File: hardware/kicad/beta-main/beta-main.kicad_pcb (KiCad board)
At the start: 4 copper layers, 76 x 121 mm, 55 parts, among them J1 FFC3A20-15-G, J10 Servo Socket, J11 Servo Socket, J12 Servo Socket, J2 FFC3A20-15-G, J3 XT60, J4 Conn_01x04_Pin, J8 Conn_01x02_Socket, J9 Servo Socket, Q2 MMBT3906, U1 MAX98357A, U2 TPS56624x, U3 AP3441SHE-7B, U6 BNO086, U7 74LVC1G126, U8 74LVC1G126

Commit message: add modifications
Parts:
- removed Module1: ComputeModule5-CM5, CM5IO:Raspberry-Pi-5-Compute-Module
- removed R14, R15: 10k, Resistor_SMD:R_0402_1005Metric
- removed U8: 74LVC1G126, Package_TO_SOT_SMD:SOT-23-5
- added C20: 10u, Capacitor_SMD:C_0603_1608Metric_Pad1.08x0.95mm_HandSolder, F.Cu at (249.1, 52.2)
- added C3: 10u, Capacitor_SMD:C_0603_1608Metric_Pad1.08x0.95mm_HandSolder, F.Cu at (240.4, 47.2)
- added C4: 10u, Capacitor_SMD:C_0603_1608Metric_Pad1.08x0.95mm_HandSolder, F.Cu at (240.4, 49.7)
- added CM5: ComputeModule5-CM5, CM5IO:Raspberry-Pi-5-Compute-Module, F.Cu at (83.5, 124.0)
- added D1: LED_RED, LED_SMD:LED_0603_1608Metric, F.Cu at (184.2, 109.0)
- added D2: 1N5819WS, Diode_SMD:D_SOD-323, F.Cu at (177.4, 113.6)
- added J13: Servo Socket, Connector_JST:JST_XH_S3B-XH-A_1x03_P2.50mm_Horizontal, F.Cu at (128.1, 150.0)
- added J14: Conn_01x04_Pin, Connector_JST:JST_PH_S4B-PH-K_1x04_P2.00mm_Horizontal, F.Cu at (69.0, 49.5)
- added J15: Conn_01x04_Pin, Connector_JST:JST_PH_S4B-PH-K_1x04_P2.00mm_Horizontal, F.Cu at (131.1, 55.5)
- added J16: Conn_01x04_Pin, Connector_JST:JST_PH_S4B-PH-K_1x04_P2.00mm_Horizontal, F.Cu at (131.1, 139.5)
- added J17: Conn_01x04_Pin, Connector_JST:JST_PH_S4B-PH-K_1x04_P2.00mm_Horizontal, F.Cu at (69.0, 133.5)
- added J18: XT60, Connector_AMASS:AMASS_XT60-F_1x02_P7.20mm_Vertical, F.Cu at (151.5, 152.5)
- added J19: FAN0, Connector_JST:JST_PH_B2B-PH-K_1x02_P2.00mm_Vertical, F.Cu at (116.0, 149.4)
- added J20: FAN1, Connector_JST:JST_PH_B2B-PH-K_1x02_P2.00mm_Vertical, F.Cu at (80.5, 149.4)
- added J21: PWR, Connector_JST:JST_PH_B2B-PH-K_1x02_P2.00mm_Vertical, F.Cu at (122.5, 50.0)
- added J5: DSI, Connector_FFC-FPC:TE_1-84953-5_1x15-1MP_P1.0mm_Horizontal, F.Cu at (130.7, 100.0)
- added J6: USB3_A, BETA:22009L012N1, F.Cu at (171.8, 77.5)
- added J7: USB3-1, Connector_JST:JST_PH_B8B-PH-K_1x08_P2.00mm_Vertical, F.Cu at (170.3, 101.8)
- added MH10: M2.5, MountingHole:MountingHole_2.7mm_Pad, F.Cu at (129.0, 75.5)
- added MH11: M2.5, MountingHole:MountingHole_2.7mm_Pad, F.Cu at (71.0, 124.5)
- added MH12: M2.5, MountingHole:MountingHole_2.7mm_Pad, F.Cu at (129.0, 124.5)
- added MH9: M2.5, MountingHole:MountingHole_2.7mm_Pad, F.Cu at (71.0, 75.5)
- added Q1: MMBT3906, Package_TO_SOT_SMD:SOT-23, F.Cu at (198.9, 54.6)
- added R10: 10K 1%, Resistor_SMD:R_0402_1005Metric, F.Cu at (260.8, 52.3)
- added R6: 100K 1%, Resistor_SMD:R_0402_1005Metric, F.Cu at (260.8, 44.4)
- added R7: 220K, Resistor_SMD:R_0402_1005Metric, F.Cu at (260.8, 46.4)
- added R8: 30K, Resistor_SMD:R_0402_1005Metric, F.Cu at (260.8, 48.4)
- added R9: 15k, Resistor_SMD:R_0402_1005Metric, F.Cu at (260.8, 50.4)
- added REF**: LayerMarker_4_6.35x2.54mm_TextH1mm_P1.27mm, Symbol:LayerMarker_4_6.35x2.54mm_TextH1mm_P1.27mm, F.Cu at (77.0, 52.5)
- added U4: 74LVC1G126, Package_TO_SOT_SMD:SOT-23-5, F.Cu at (69.1, 103.0)
- added U5: AP3441SHE-7B, Package_DFN_QFN:DFN-8-1EP_2x2mm_P0.5mm_EP1.05x1.75mm, F.Cu at (110.9, 144.2)
- C1: value 220u -> 0.1u
- C10: value 22u -> 4.7nF; footprint Capacitor_SMD:C_0603_1608Metric_Pad1.08x0.95mm_HandSolder -> Capacitor_SMD:C_0402_1005Metric
- C12: value 10u -> 100u
- C14: value 0.1u -> 22u; footprint Capacitor_SMD:C_0402_1005Metric -> Capacitor_SMD:C_0603_1608Metric_Pad1.08x0.95mm_HandSolder
- C15: value 4.7nF -> 10u; footprint Capacitor_SMD:C_0402_1005Metric -> Capacitor_SMD:C_0603_1608Metric_Pad1.08x0.95mm_HandSolder
- C17, C19: value 10u -> 22u
- C2: value 0.1u -> 220u
- C8: value 22u -> 0.1u; footprint Capacitor_SMD:C_0603_1608Metric_Pad1.08x0.95mm_HandSolder -> Capacitor_SMD:C_0402_1005Metric
- C9: value 22u -> 10u
- J1: value FFC3A20-15-G -> AUDIO; footprint Connector_FFC-FPC:TE_1-84953-5_1x15-1MP_P1.0mm_Horizontal -> Connector_JST:JST_PH_B2B-PH-K_1x02_P2.00mm_Vertical
- J10, J11, J12: footprint Connector_JST:JST_XH_B3B-XH-AM_1x03_P2.50mm_Vertical -> Connector_JST:JST_XH_S3B-XH-A_1x03_P2.50mm_Horizontal
- J2: value FFC3A20-15-G -> USB3-0; footprint Connector_FFC-FPC:TE_1-84953-5_1x15-1MP_P1.0mm_Horizontal -> Connector_JST:JST_PH_B8B-PH-K_1x08_P2.00mm_Vertical
- J3: value XT60 -> USB3-1; footprint Connector_AMASS:AMASS_XT60-F_1x02_P7.20mm_Vertical -> Connector_JST:JST_PH_B8B-PH-K_1x08_P2.00mm_Vertical
- J4: value Conn_01x04_Pin -> USB3-1; footprint Connector_JST:JST_XH_B4B-XH-AM_1x04_P2.50mm_Vertical -> Connector_JST:JST_PH_B8B-PH-K_1x08_P2.00mm_Vertical
- J8: value Conn_01x02_Socket -> CSI; footprint Connector_PinHeader_2.54mm:PinHeader_1x02_P2.54mm_Vertical -> Connector_FFC-FPC:TE_1-84953-5_1x15-1MP_P1.0mm_Horizontal
- J9: value Servo Socket -> USB3_A; footprint Connector_JST:JST_XH_B3B-XH-AM_1x03_P2.50mm_Vertical -> BETA:22009L012N1
- Q2: value MMBT3906 -> IRLML6246TRP
- R1: value 220K -> 20k
- R11: value 20k -> 2.2K 1%
- R12: value 10k -> 1k; footprint Resistor_SMD:R_0402_1005Metric -> Resistor_SMD:R_0603_1608Metric
- R13: footprint Resistor_SMD:R_0402_1005Metric -> Resistor_SMD:R_0603_1608Metric
- R2: value 30K -> 10k
- R3: value 100K 1% -> 10k
- R4: value 10K 1% -> 10k
- R5: value 2.2K 1% -> 10k
- U2: value TPS56624x -> 74LVC1G126; footprint Package_TO_SOT_SMD:SOT-563 -> Package_TO_SOT_SMD:SOT-23-5
- U3: value AP3441SHE-7B -> BNO086; footprint Package_DFN_QFN:DFN-8-1EP_2x2mm_P0.5mm_EP1.05x1.75mm -> BETA:IC_BNO086
- U6: value BNO086 -> TPS56624x; footprint BNO086:IC_BNO086 -> Package_TO_SOT_SMD:SOT-563
- U7: value 74LVC1G126 -> AP2553W6; footprint Package_TO_SOT_SMD:SOT-23-5 -> Package_TO_SOT_SMD:SOT-23-6
- moved TP2 201.8 mm to (257.3, 37.7)
- moved C17 192.6 mm to (249.1, 44.6), turned to 0 degrees
- moved C18 192.1 mm to (249.1, 47.2), turned to 0 degrees
- moved C19 191.5 mm to (249.1, 49.7), turned to 0 degrees
- moved C12 188.3 mm to (244.8, 47.2), turned to 0 degrees
- moved R11 187.8 mm to (260.8, 54.3), turned to 0 degrees
- moved C13 185.2 mm to (244.8, 49.7), turned to 0 degrees
- moved L2 184.0 mm to (255.3, 54.1)
- moved C14 183.7 mm to (244.8, 52.2)
- moved C10 182.3 mm to (260.3, 38.1), turned to 0 degrees
- moved C16 181.7 mm to (244.8, 57.2), turned to 0 degrees
- moved C8 181.7 mm to (260.3, 36.1), turned to 0 degrees
- moved C15 180.8 mm to (244.8, 54.7)
- moved TP1 178.2 mm to (257.3, 34.7)
- moved C7 174.6 mm to (260.3, 34.1), turned to 0 degrees
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- renumbered MH2 to MH3, MH3 to MH5, MH4 to MH7
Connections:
- C1 pad 1: +BATT -> GND
- C1 pad 2: GND -> Net-(U3-CAP)
- C10 pad 1: +5V -> +3V3
- C10 pad 2: GND -> /PSU/FB
- C12 pad 1: +5V -> VBUS
- C13 pad 1: +5V -> +3V3
- C15 pad 1: +3V3 -> VBUS
- C15 pad 2: /PSU/3V3/FB -> GND
- C17 pad 1: +3V3 -> +5V
- C19 pad 1: +3V3 -> +5V
- C2 pad 1: GND -> +BATT
- C2 pad 2: Net-(U6-CAP) -> GND
- C5 pad 1: +BATT -> +5V
- C7 pad 1: +BATT -> +5V
- C8 pad 1: +5V -> +BATT
- J1 pad 1: GND -> Net-(J1-Pin_1)
- J1 pad 2: /CM5/MIPI0_D1_N -> Net-(J1-Pin_2)
- J10 pad 1: Net-(J10-Pin_1) -> /Peripherals/SIG
- J11 pad 1: Net-(J10-Pin_1) -> /Peripherals/SIG
- J12 pad 1: Net-(J10-Pin_1) -> /Peripherals/SIG
- J2 pad 1: GND -> VBUS
- J2 pad 2: /CM5/MIPI1_D0_N -> /High Speed Serial/USB3-0-D_N
- J2 pad 3: /CM5/MIPI1_D0_P -> /High Speed Serial/USB3-0-D_P
- J2 pad 4: GND -> /High Speed Serial/USB3-0-RX_N
- J2 pad 5: /CM5/MIPI1_D1_N -> /High Speed Serial/USB3-0-RX_P
- J2 pad 6: /CM5/MIPI1_D1_P -> /High Speed Serial/USB3-0-TX_N
- J2 pad 7: GND -> /High Speed Serial/USB3-0-TX_P
- J2 pad 8: /CM5/MIPI1_C_N -> GND
- J3 pad 1: GND -> VBUS
- J3 pad 2: +BATT -> /High Speed Serial/USB3-1-D_N
- J4 pad 1: unconnected-(J4-Pin_1-Pad1) -> Net-(J4-Pin_1)
- J4 pad 2: unconnected-(J4-Pin_2-Pad2) -> Net-(J4-Pin_2)
- J4 pad 3: unconnected-(J4-Pin_3-Pad3) -> Net-(J4-Pin_3)
- J4 pad 4: unconnected-(J4-Pin_4-Pad4) -> Net-(J4-Pin_4)
- J8 pad 1: Net-(J8-Pin_1) -> GND
- J8 pad 2: Net-(J8-Pin_2) -> /MIPI1_D0_N
- J9 pad 1: Net-(J10-Pin_1) -> Net-(J7-Pin_1)
- J9 pad 2: +BATT -> Net-(J7-Pin_2)
- J9 pad 3: GND -> Net-(J7-Pin_3)
- L1 pad 1: Net-(U2-SW) -> Net-(U6-SW)
- L2 pad 1: Net-(U3-LX) -> Net-(U5-LX)
- Q2 pad 1: Net-(Q2-B) -> /GPIO/FAN_PWM
- Q2 pad 2: +3V3 -> Net-(D2-K)
- Q2 pad 3: /CM5/Servo Controller/TXEN -> GND
- R1 pad 1: +5V -> GND
- R1 pad 2: Net-(U2-FB) -> /Peripherals/TXEN
- R11 pad 1: GND -> /PSU/FB
- R11 pad 2: /CM5/Servo Controller/TXEN -> GND
- R12 pad 1: Net-(Q2-B) -> Net-(D1-K)
- R12 pad 2: /CM5/UART3_RX -> Net-(CM5A-LED_nACT)
- R13 pad 1: +3V3 -> /GPIO/FAN_PWM
- R13 pad 2: /CM5/UART3_RX -> GND
- R2 pad 1: Net-(U2-FB) -> Net-(Q1-B)
- R2 pad 2: GND -> /GPIO/UART3_TX
- R3 pad 1: +5V -> +3V3
- R3 pad 2: GND -> /GPIO/UART3_TX
- R4 pad 2: /PSU/3V3/FB -> /Peripherals/SIG
- R5 pad 1: /PSU/3V3/FB -> +3V3
- R5 pad 2: GND -> /GPIO/UART3_RX
- U1 pad 1: /CM5/I2S0_SDO -> /I2S0_SDO
- U1 pad 10: Net-(J8-Pin_2) -> Net-(J1-Pin_2)
- U1 pad 14: /CM5/I2S0_WS -> /I2S0_WS
- U1 pad 16: /CM5/I2S0_SCLK -> /I2S0_SCLK
- U1 pad 9: Net-(J8-Pin_1) -> Net-(J1-Pin_1)
- U2 pad 1: +BATT -> /Peripherals/TXEN
- U2 pad 2: Net-(U2-SW) -> /GPIO/UART3_TX
- U2 pad 4: GND -> /Peripherals/SIG
- U2 pad 5: +BATT -> +3V3
- U3 pad 1: /PSU/3V3/FB -> unconnected-(U3-RESV_NC-Pad1)
- U3 pad 2: unconnected-(U3-PG-Pad2) -> GND
- U3 pad 3: +5V -> +3V3
- U3 pad 4: GND -> +3V3
- U3 pad 5: unconnected-(U3-nc-Pad5) -> GND
- U3 pad 6: Net-(U3-LX) -> GND
- U3 pad 7: +5V -> unconnected-(U3-RESV_NC-Pad7)
- U3 pad 8: GND -> unconnected-(U3-RESV_NC-Pad8)
- U3 pad 9: GND -> Net-(U3-CAP)
- U6 pad 1: unconnected-(U6-RESV_NC-Pad1) -> +BATT
- U6 pad 2: GND -> Net-(U6-SW)
- U6 pad 3: +3V3 -> GND
- U6 pad 4: +3V3 -> GND
- U6 pad 5: GND -> +BATT
- U6 pad 6: GND -> Net-(U6-FB)
- U7 pad 1: /CM5/Servo Controller/TXEN -> +5V
- U7 pad 2: /CM5/UART3_RX -> GND
- U7 pad 3: GND -> /VBUS_EN
- U7 pad 4: Net-(J10-Pin_1) -> unconnected-(U7-nFault-Pad4)
- U7 pad 5: +3V3 -> Net-(U7-ILIM)
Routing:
- net /MIPI0_D1_P: track 0.00 -> 0.73 mm
- net /MIPI0_D1_N: track 0.00 -> 0.73 mm
- added copper zone on In2.Cu, net +BATT
- added copper zone on B.Cu, net GND
- added copper zone on F.Cu, net GND
- added copper zone on In1.Cu, net GND
- added copper zone on In2.Cu, net GND
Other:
- board size 76 x 121 mm -> 76 x 148 mm
- rule pad_to_mask_clearance: 0.1 -> 0

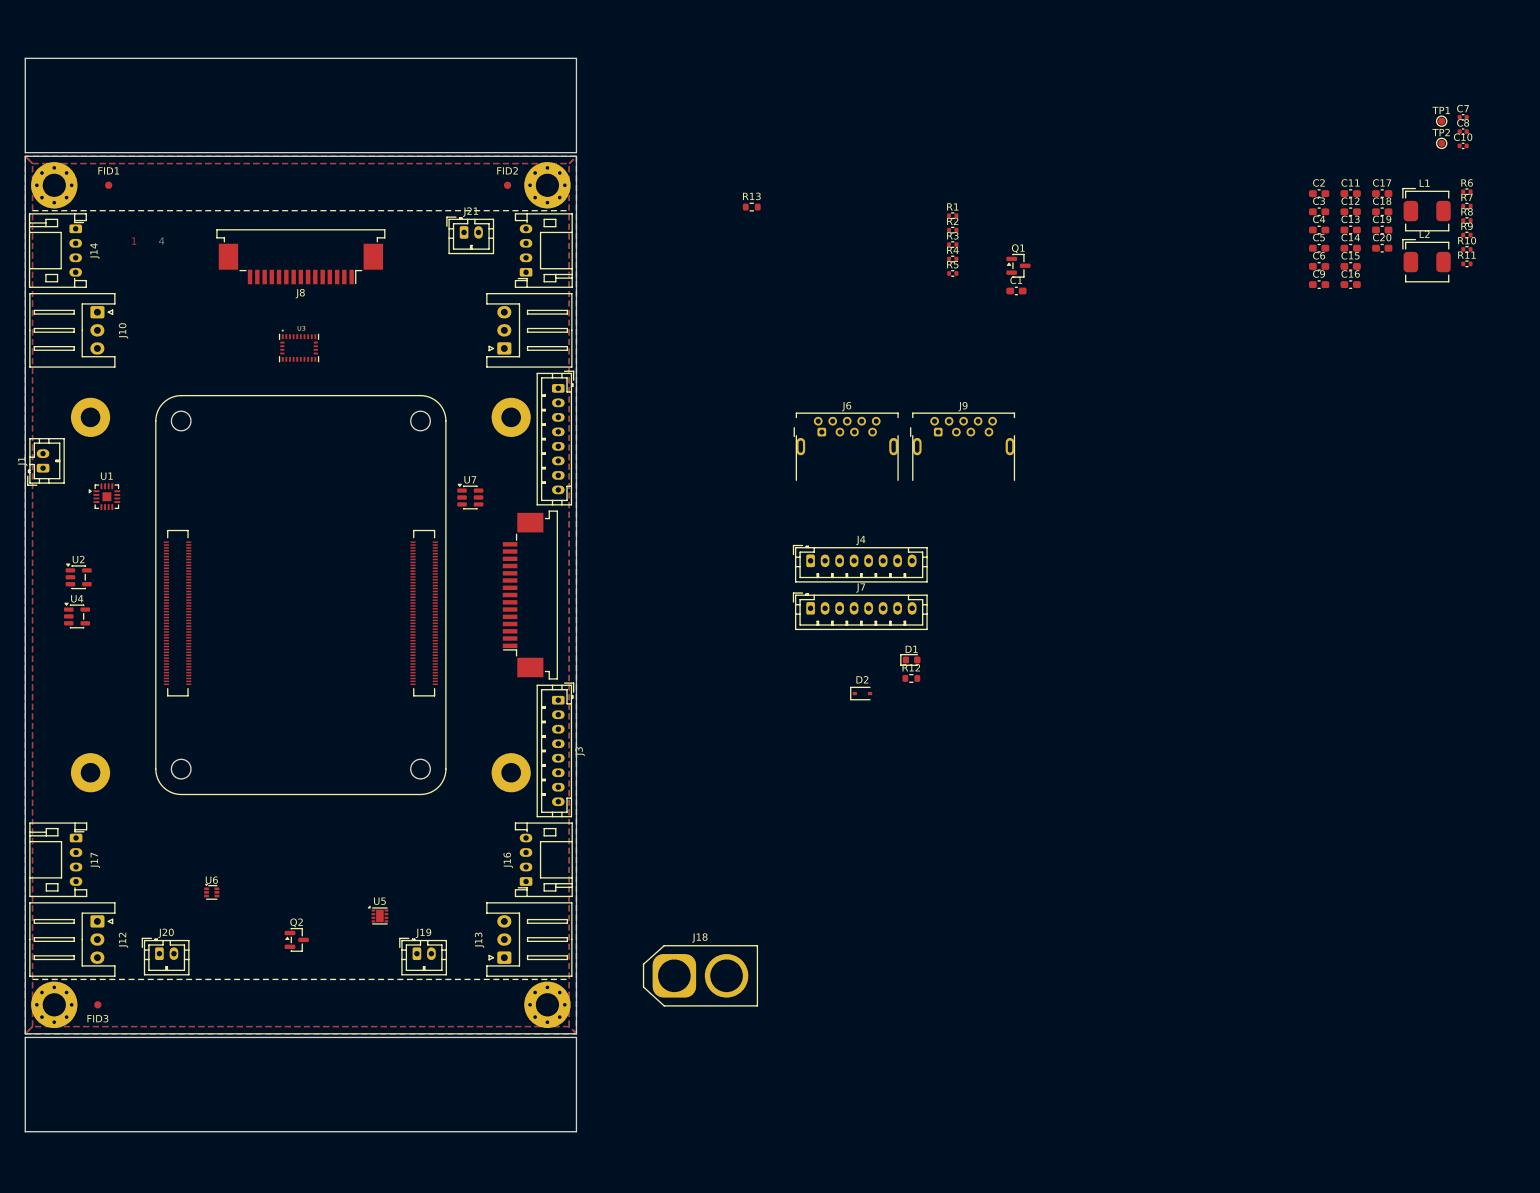
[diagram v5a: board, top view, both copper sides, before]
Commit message: add filled zones and layout 5V and 3V3
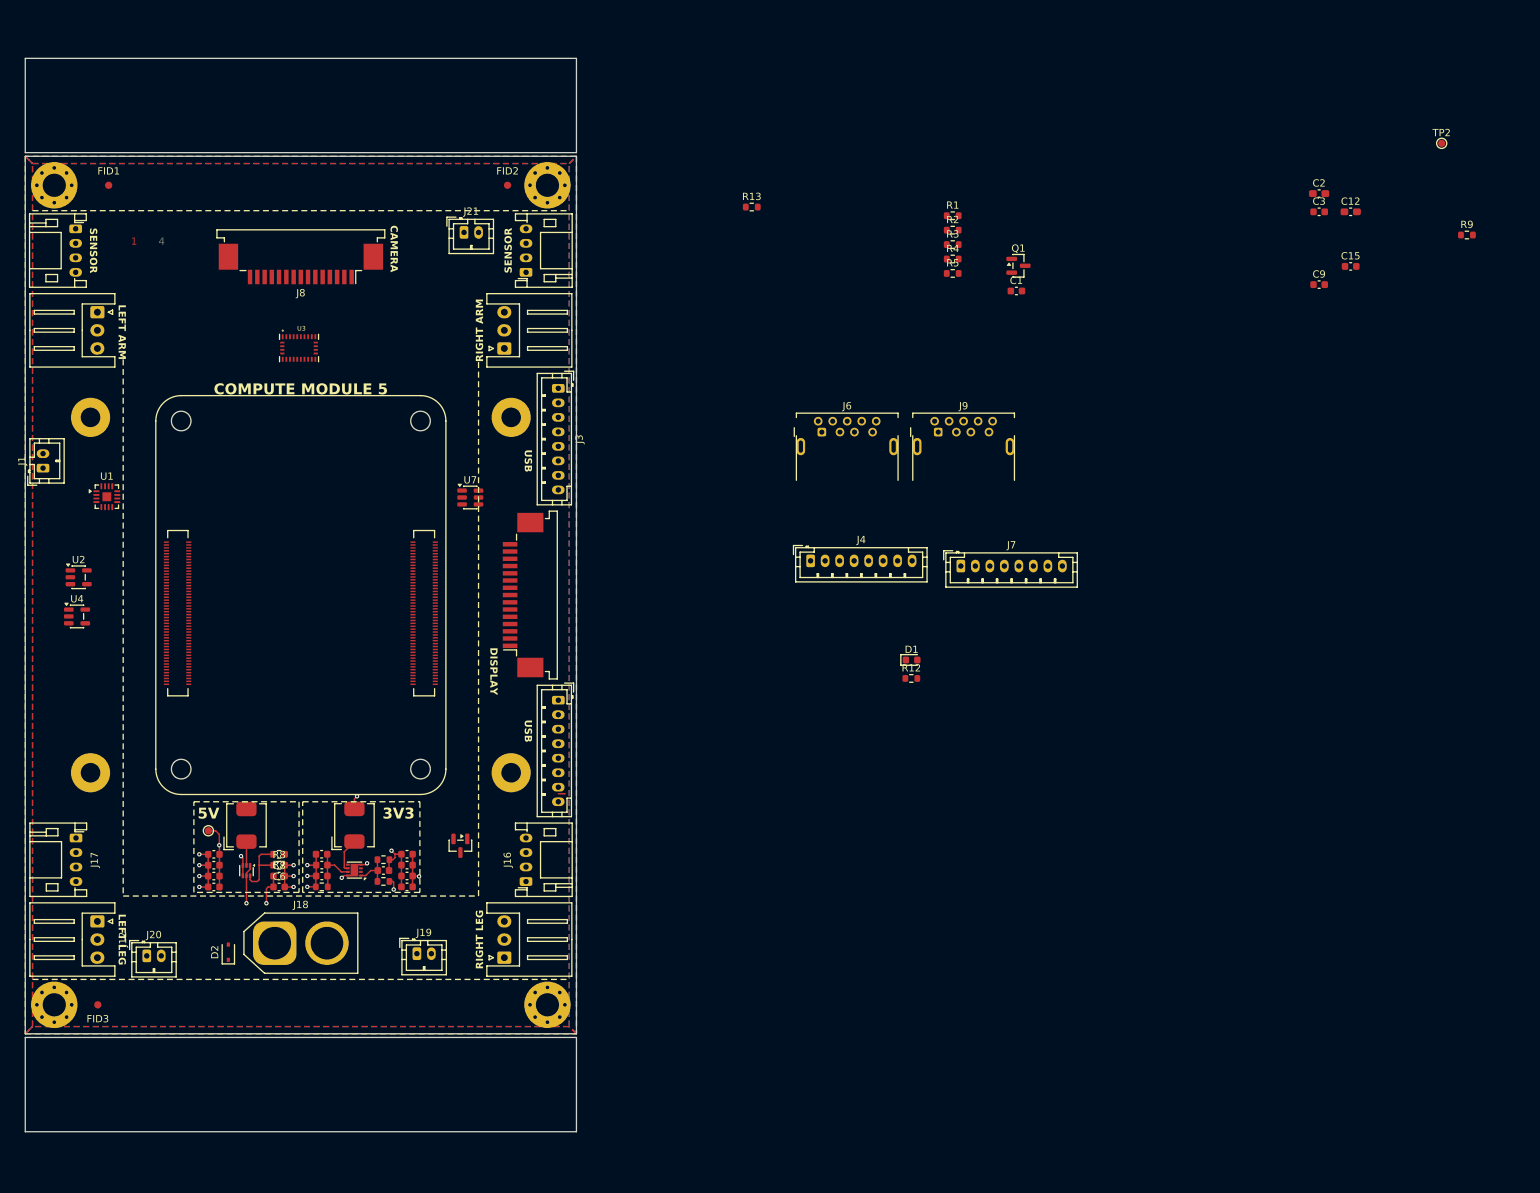
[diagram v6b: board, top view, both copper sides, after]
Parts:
- C1, C11, C13, C14, C15, C16, C17, C18, C19, C20, C3, C4, C5, C6, C9: footprint Capacitor_SMD:C_0603_1608Metric_Pad1.08x0.95mm_HandSolder -> Capacitor_SMD:C_0603_1608Metric
- C10, C7, C8: footprint Capacitor_SMD:C_0402_1005Metric -> Capacitor_SMD:C_0603_1608Metric
- R1, R10, R11, R2, R3, R4, R5, R6, R7, R8, R9: footprint Resistor_SMD:R_0402_1005Metric -> Resistor_SMD:R_0603_1608Metric
- moved TP1 196.2 mm to (87.2, 132.5)
- moved C8 192.9 mm to (97.0, 138.8)
- moved C7 188.1 mm to (102.9, 137.2), turned to 180 degrees
- moved R7 186.6 mm to (97.0, 135.8), turned to 180 degrees
- moved C17 186.6 mm to (88.0, 138.8), turned to 180 degrees
- moved R8 186.3 mm to (97.0, 137.2)
- moved C19 184.8 mm to (88.0, 140.2), turned to 180 degrees
- moved R6 184.7 mm to (102.9, 140.2), turned to 180 degrees
- moved L1 183.5 mm to (92.5, 131.8), turned to 90 degrees
- moved C11 181.3 mm to (88.0, 135.8), turned to 180 degrees
- moved C10 179.3 mm to (111.4, 138.0), turned to 180 degrees
- moved C14 178.4 mm to (88.0, 137.2), turned to 180 degrees
- moved R11 172.0 mm to (111.4, 139.5)
- moved R10 171.5 mm to (111.4, 136.5), turned to 180 degrees
- moved L2 167.1 mm to (107.4, 131.7), turned to 90 degrees
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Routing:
- net GND: track 0.00 -> 38.7 mm, vias 0 -> 15
- net +5V: track 0.00 -> 16.7 mm, vias 0 -> 1
- net +3V3: track 0.00 -> 10.8 mm, vias 0 -> 2
- net +BATT: track 0.00 -> 10.00 mm, vias 0 -> 2
- net Net-(U6-FB): track 0.00 -> 9.20 mm
- net /PSU/FB: track 0.00 -> 5.65 mm
- net Net-(U5-LX): track 0.00 -> 4.71 mm
- net Net-(U6-SW): track 0.00 -> 2.79 mm
- net (no net): track 0.00 -> 0.90 mm
- added copper zone on In2.Cu, net +3V3
- added copper zone on In2.Cu, net +5V
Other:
- board text added: "3V3"
- board text added: "5V"
- board text added: "CAMERA"
- board text added: "COMPUTE MODULE 5"
- board text added: "DISPLAY"
- board text added: "LEFT ARM"
- board text added: "LEFT LEG"
- board text added: "RIGHT ARM"
- board text added: "RIGHT LEG"
- board text added: "SENSOR"
- board text added: "USB"

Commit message: add fan control
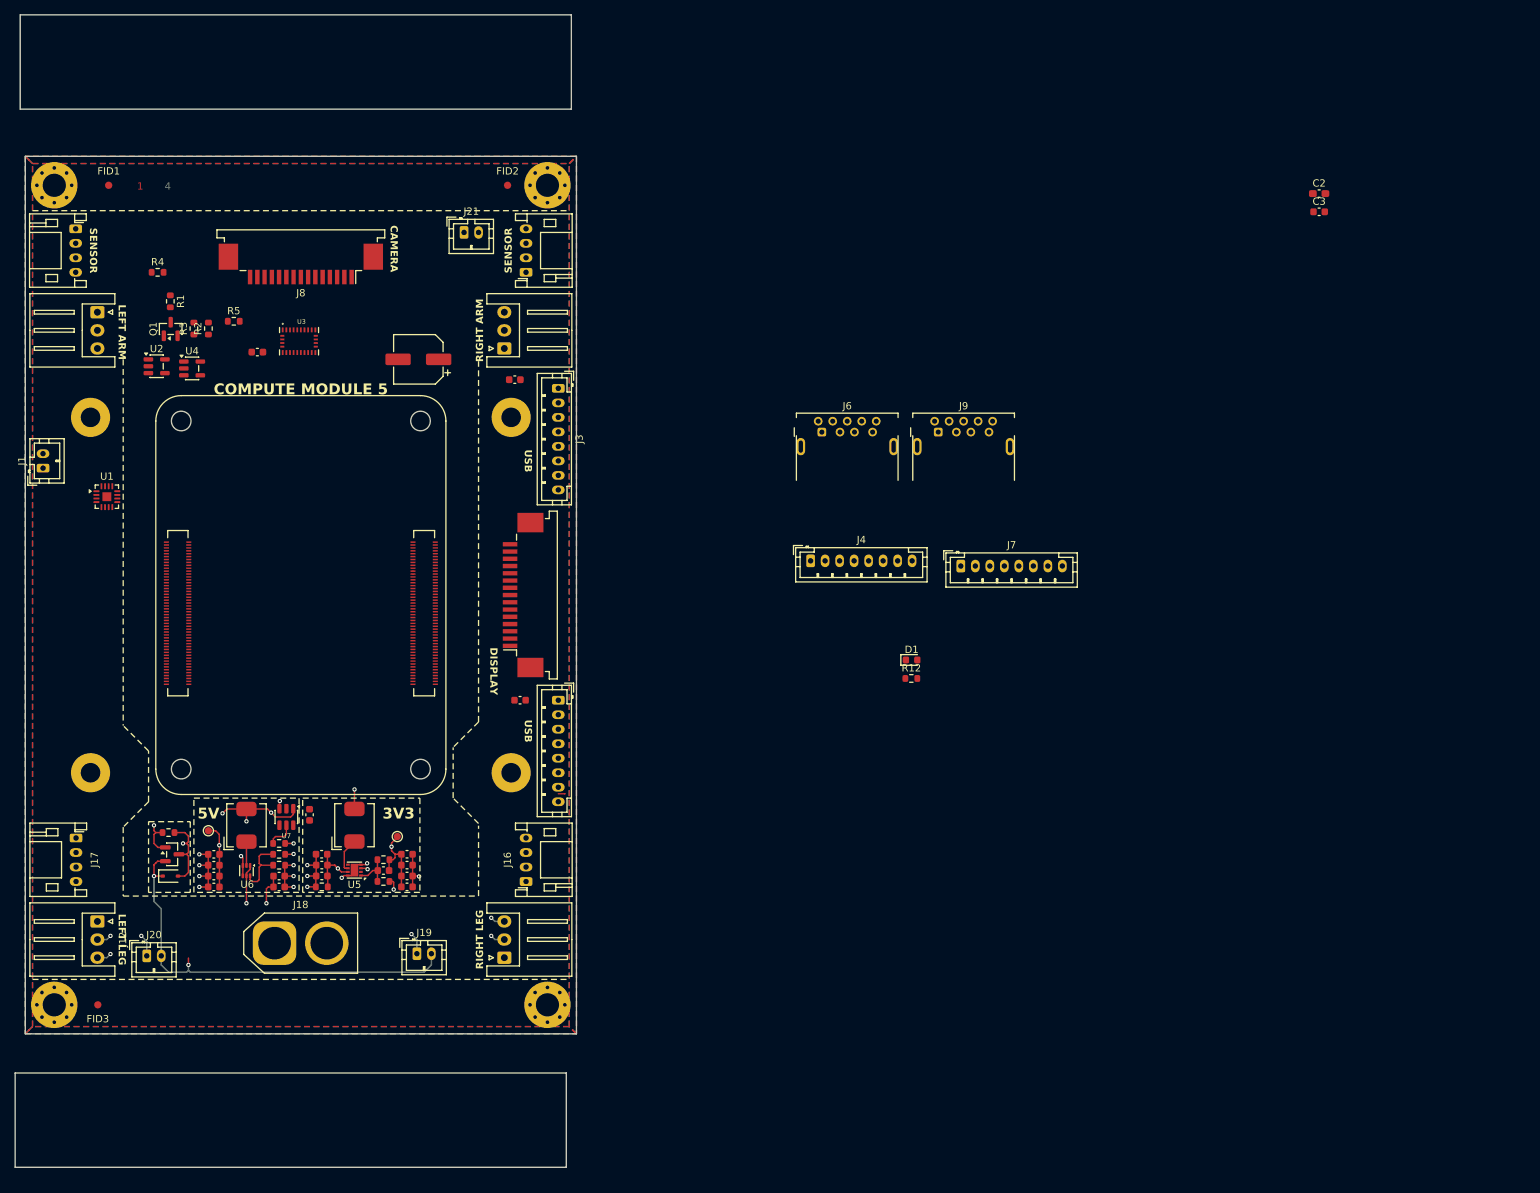
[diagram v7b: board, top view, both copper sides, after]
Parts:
- added C21: 10u, Capacitor_SMD:C_0603_1608Metric, F.Cu at (129.5, 70.3)
- C12: footprint Capacitor_SMD:C_0603_1608Metric_Pad1.08x0.95mm_HandSolder -> Capacitor_SMD:CP_Elec_6.3x5.9
- moved R9 184.0 mm to (97.0, 134.2)
- moved TP2 172.8 mm to (113.3, 133.3)
- moved C9 157.2 mm to (101.2, 130.3), turned to -90 degrees
- moved C12 130.2 mm to (116.2, 67.5), turned to 180 degrees
- moved C15 129.2 mm to (130.2, 114.5), turned to 180 degrees
- moved R13 117.9 mm to (81.8, 132.8)
- moved Q1 117.2 mm to (82.0, 63.3), turned to 90 degrees
- moved R4 109.7 mm to (80.2, 55.5)
- moved R1 108.5 mm to (82.0, 59.5), turned to -90 degrees
- moved R3 105.3 mm to (85.2, 63.2), turned to 90 degrees
- moved C1 105.0 mm to (94.0, 66.5)
- moved R2 103.5 mm to (87.2, 63.2), turned to 90 degrees
- moved R5 99.4 mm to (90.8, 62.2)
- moved U7 50.8 mm to (98.0, 130.6), turned to -90 degrees
- moved Q2 39.8 mm to (82.2, 135.8), turned to 0 degrees
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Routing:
- net Net-(D2-K): track 0.00 -> 58.7 mm, vias 0 -> 2
- net GND: track 38.7 -> 54.7 mm, vias 15 -> 19
- net +5V: track 16.7 -> 32.6 mm, vias 1 -> 7
- net +BATT: track 10.00 -> 20.1 mm, vias 2 -> 6
- net /GPIO/FAN_PWM: track 0.00 -> 5.42 mm, vias 0 -> 1
- net Net-(U7-ILIM): track 0.00 -> 3.97 mm
- net +3V3: track 10.8 -> 13.9 mm
- net /VBUS_EN: track 0.00 -> 1.08 mm, vias 0 -> 1
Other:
- board size 76 x 148 mm -> 77.4 x 158.9 mm
